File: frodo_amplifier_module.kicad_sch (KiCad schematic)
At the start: 35 parts, among them IC1 MCP3221A5T-I_OT, IC2 INA826AID, J1 Conn_01x01_Socket, J2 Conn_01x01_Socket, J3 Conn_01x01_Socket, J4 Conn_01x01_Socket, J5 Conn_01x01_Socket, J6 Conn_01x01_Socket, J7 Conn_01x01_Socket, J8 Conn_01x01_Socket, U1 MCP602, U2 MIC5504-3.3YM5

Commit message: finished the scematics
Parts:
- removed C9: 0u1, Capacitor_SMD:C_0402_1005Metric, symbol Device:C
- removed IC1: MCP3221A5T-I_OT, Package_TO_SOT_SMD:SOT-23-5, symbol MCP3221A5T-I_OT:MCP3221A5T-I_OT
- removed J1, J2, J3, J4, J5, J6, J7, J8: Conn_01x01_Socket, Connector_Wire:SolderWirePad_1x01_SMD_1x2mm, symbol Connector:Conn_01x01_Socket
- removed R2: 10k, Resistor_SMD:R_0402_1005Metric, symbol Device:R
- removed U1: MCP602, Package_SO:SOIC-8-1EP_3.9x4.9mm_P1.27mm_EP2.29x3mm, symbol Amplifier_Operational:MCP602
- added C11: 470n, Capacitor_SMD:C_0402_1005Metric, symbol Device:C
- added C12, C13: 0u1, Capacitor_SMD:C_0402_1005Metric, symbol Device:C
- added C5: 10n, Capacitor_SMD:C_0402_1005Metric, symbol Device:C
- added C6: 2n2, Capacitor_SMD:C_0402_1005Metric, symbol Device:C
- added J? (x4): JST-GH, Connector_JST:JST_GH_BM04B-GHS-TBT_1x04-1MP_P1.25mm_Vertical, symbol Connector_Generic_MountingPin:Conn_01x04_MountingPin
- added JP2, JP3: SolderJumper_3_Open, Jumper:SolderJumper-3_P1.3mm_Open_RoundedPad1.0x1.5mm, symbol Jumper:SolderJumper_3_Open
- added R4: 10k, Resistor_SMD:R_0402_1005Metric_Pad0.72x0.64mm_HandSolder, symbol Device:R
- added U1: ADC101C021CIMM, Package_SO:SSOP-8_2.95x2.8mm_P0.65mm, symbol Analog_ADC:ADC101C021CIMM
- added U2: MCP6001-OT, Package_TO_SOT_SMD:SOT-23-5, symbol Amplifier_Operational:MCP6001-OT
- added U4: REF3033, Package_TO_SOT_SMD:SOT-23, symbol Reference_Voltage:REF3033
- C1: footprint Capacitor_SMD:C_0603_1608Metric -> Capacitor_SMD:C_0402_1005Metric
- C3: value 10u -> 4u7; footprint Capacitor_SMD:C_0603_1608Metric -> Capacitor_SMD:C_0402_1005Metric
- FB1, FB2: footprint Inductor_SMD:L_0603_1608Metric -> Inductor_SMD:L_0402_1005Metric
- IC1: renamed from IC2; footprint Package_SO:SOIC-8_3.9x4.9mm_P1.27mm -> Package_SON:WSON-8-1EP_3x3mm_P0.5mm_EP1.2x2mm
- JP1: footprint Jumper:SolderJumper-3_P1.3mm_Open_RoundedPad1.0x1.5mm_NumberLabels -> Jumper:SolderJumper-3_P1.3mm_Open_RoundedPad1.0x1.5mm
- R1: footprint Resistor_SMD:R_0402_1005Metric_Pad0.72x0.64mm_HandSolder -> Resistor_SMD:R_0402_1005Metric
- R3: value 10k -> 5k; footprint Resistor_SMD:R_0402_1005Metric -> Resistor_SMD:R_0402_1005Metric_Pad0.72x0.64mm_HandSolder
- RG1: footprint Resistor_SMD:R_0603_1608Metric_Pad0.98x0.95mm_HandSolder -> Resistor_SMD:R_0603_1608Metric
- renumbered C8 to C10, C10 to C14, C11 to C15, C12 to C16, C5 to C7, C6 to C8, C7 to C9, JP2 to JP4, R4 to R2, U2 to U3
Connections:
- net +IN: now also J?.3 (Pin_3)
- net -IN: now also J?.2 (Pin_2)
- net 3V3: now also C8.1, J?.4 (Pin_4), JP2.3 (B), JP3.3 (B); no longer C3.1, C4.1, JP1.3 (B), R3.1, R5.2
- net 5V: now also C11.1, C12.1, C5.1, J?.4 (Pin_4), U4.1 (IN); no longer JP1.2 (C)
- net GND: now also C11.2, C12.2, C13.2, C5.2, C6.2, J?.1 (Pin_1), J?.1 (Pin_1), J?.2 (Pin_2), JP2.1 (A), JP3.1 (A), R4.1, U1.7 (GND), U2.2 (V-), U4.3 (GND)
- net SCL: now also J?.3 (Pin_3), J?.3 (Pin_3), U1.8 (SDA); no longer R3.2
- net SDA: now also J?.2 (Pin_2), J?.2 (Pin_2), U1.1 (SCL)
- net sig: now also JP1.3 (B)
- net sig2: now reaches JP1.1 (A)
- net sig2: now also R3.1, R4.2; no longer C8.1
- net at FB2.1: now also J?.1 (Pin_1), J?.1 (Pin_1)
- net at R5.1, R6.2: now also U2.3 (+)
- net at JP4.3 (B): now also U2.1, U2.4 (-)
- net at FB1.1: now also J?.4 (Pin_4), J?.4 (Pin_4)
- new net: JP2.2 (C), U1.3 (ADR0)
- new net: JP1.2 (C), U1.4 (VIN)
- new net: JP3.2 (C), U1.6 (ADR1)
- new net: C6.1, J?.3 (Pin_3), R3.2
- new net 3V3Ref: C13.1, C3.1, C4.1, R5.2, U1.5 (VA), U2.5 (V+), U4.2 (OUT)
- no-connect marks 0 -> 1
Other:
- note added: "pullup resistors, typically: - 10 kΩ for 100 kHz - 2 kΩ for 400 kHz SCL clock speeds -> already on io board (4.7k) -> so not neccesarry"
- note added: "to next amp board"
- note added: "to sensor (3.3V)"
- note added: "to sensor 5V"
- note removed: "possibility to supply 5V (may be neccesarry for some sensors)"
- note removed: "pullup resistors, typically: - 10 kΩ for 100 kHz - 2 kΩ for 400 kHz SCL clock speeds"
- note removed: "to sensor"
- moved on the sheet: C1, C10, C14, C15, C16, C2, C3, C4, C7, C8, C9, FB1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

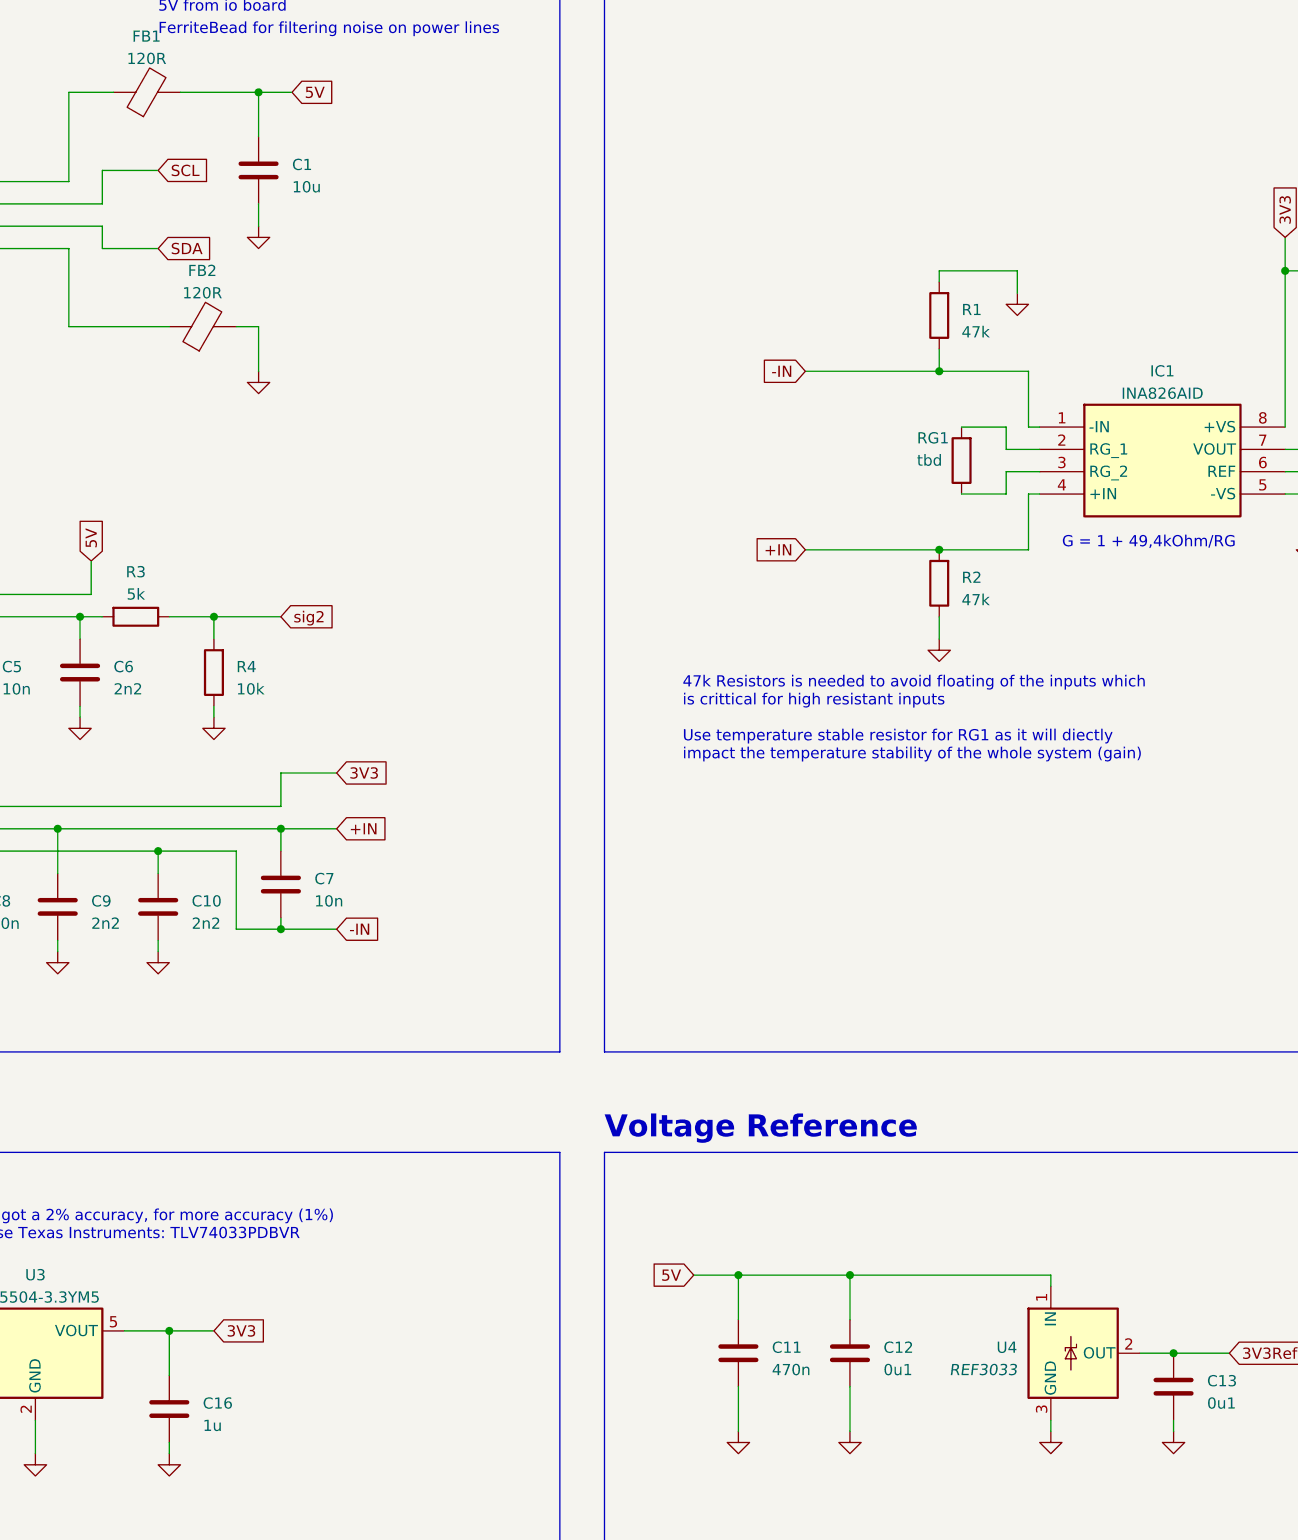
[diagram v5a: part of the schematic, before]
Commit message: started the pcb layout for the amp module
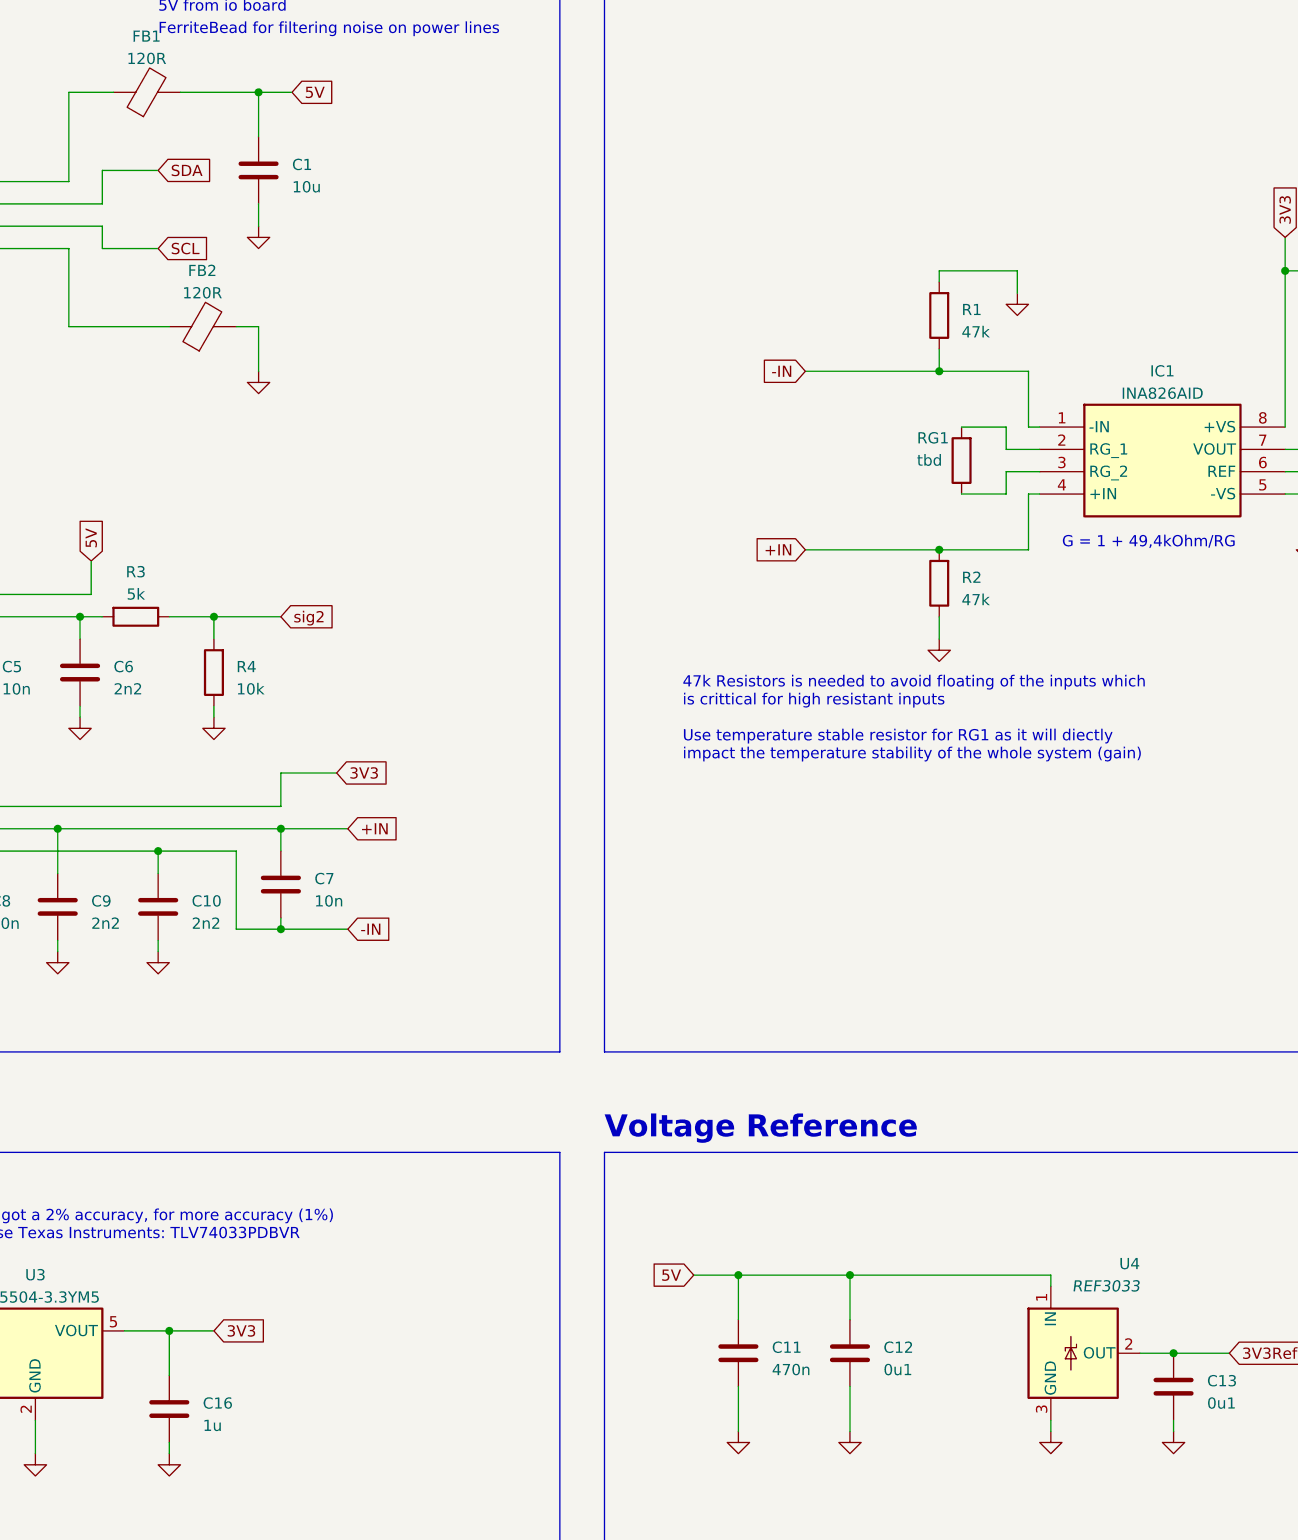
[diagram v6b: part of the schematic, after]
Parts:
- J? (x4): footprint Connector_JST:JST_GH_BM04B-GHS-TBT_1x04-1MP_P1.25mm_Vertical -> Connector_JST:JST_GH_SM04B-GHS-TB_1x04-1MP_P1.25mm_Horizontal
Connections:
- net SCL: now also J?.2 (Pin_2), J?.2 (Pin_2); no longer J?.3 (Pin_3), J?.3 (Pin_3)
- net SDA: now also J?.3 (Pin_3), J?.3 (Pin_3); no longer J?.2 (Pin_2), J?.2 (Pin_2)
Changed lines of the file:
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@@
     (stroke (width 0) (type default))
   )
-  (wire (pts (xy 100.33 138.43) (xy 106.68 138.43))
+  (wire (pts (xy 100.33 138.43) (xy 107.95 138.43))
     (stroke (width 0) (type default))
   )
@@
     (stroke (width 0) (type default))
   )
-  (wire (pts (xy 100.33 127) (xy 106.68 127))
+  (wire (pts (xy 100.33 127) (xy 107.95 127))
     (stroke (width 0) (type default))
   )
@@
     )
   )
-  (global_label "SCL" (shape input) (at 86.36 52.07 0) (fields_autoplaced)
-    (effects (font (size 1.27 1.27)) (justify left))
-    (property "Intersheetrefs" "${INTERSHEET_REFS}" (at 92.7734 52.07 0)
-      (effects (font (size 1.27 1.27)) (justify left) hide)
-    )
-  )
   (global_label "SCL" (shape input) (at 336.55 87.63 0) (fields_autoplaced)
     (effects (font (size 1.27 1.27)) (justify left))
@@
     )
   )
-  (global_label "-IN" (shape input) (at 106.68 138.43 0) (fields_autoplaced)
-    (effects (font (size 1.27 1.27)) (justify left))
-    (property "Intersheetrefs" "${INTERSHEET_REFS}" (at 113.0935 138.43 0)
-      (effects (font (size 1.27 1.27)) (justify left) hide)
-    )
-  )
   (global_label "sig2" (shape input) (at 257.81 87.63 180) (fields_autoplaced)
     (effects (font (size 1.27 1.27)) (justify right))
@@
     )
   )
+  (global_label "-IN" (shape input) (at 107.95 138.43 0) (fields_autoplaced)
+    (effects (font (size 1.27 1.27)) (justify left))
+    (property "Intersheetrefs" "${INTERSHEET_REFS}" (at 114.3635 138.43 0)
+      (effects (font (size 1.27 1.27)) (justify left) hide)
+    )
+  )
   (global_label "ref" (shape input) (at 227.33 87.63 0) (fields_autoplaced)
     (effects (font (size 1.27 1.27)) (justify left))
@@
     )
   )
+  (global_label "SCL" (shape input) (at 86.36 60.96 0) (fields_autoplaced)
+    (effects (font (size 1.27 1.27)) (justify left))
+    (property "Intersheetrefs" "${INTERSHEET_REFS}" (at 92.7734 60.96 0)
+      (effects (font (size 1.27 1.27)) (justify left) hide)
+    )
+  )
+  (global_label "SDA" (shape input) (at 86.36 52.07 0) (fields_autoplaced)
+    (effects (font (size 1.27 1.27)) (justify left))
+    (property "Intersheetrefs" "${INTERSHEET_REFS}" (at 92.8339 52.07 0)
+      (effects (font (size 1.27 1.27)) (justify left) hide)
+    )
+  )
   (global_label "SDA" (shape input) (at 336.55 82.55 0) (fields_autoplaced)
     (effects (font (size 1.27 1.27)) (justify left))
@@
     )
   )
-  (global_label "SDA" (shape input) (at 86.36 60.96 0) (fields_autoplaced)
-    (effects (font (size 1.27 1.27)) (justify left))
-    (property "Intersheetrefs" "${INTERSHEET_REFS}" (at 92.8339 60.96 0)
-      (effects (font (size 1.27 1.27)) (justify left) hide)
-    )
-  )
   (global_label "sig2" (shape input) (at 100.33 102.87 0) (fields_autoplaced)
     (effects (font (size 1.27 1.27)) (justify left))
@@
     )
   )
-  (global_label "+IN" (shape input) (at 106.68 127 0) (fields_autoplaced)
-    (effects (font (size 1.27 1.27)) (justify left))
-    (property "Intersheetrefs" "${INTERSHEET_REFS}" (at 113.0935 127 0)
-      (effects (font (size 1.27 1.27)) (justify left) hide)
-    )
-  )
   (global_label "ref" (shape input) (at 269.24 196.85 0) (fields_autoplaced)
     (effects (font (size 1.27 1.27)) (justify left))
@@
     )
   )
+  (global_label "+IN" (shape input) (at 107.95 127 0) (fields_autoplaced)
+    (effects (font (size 1.27 1.27)) (justify left))
+    (property "Intersheetrefs" "${INTERSHEET_REFS}" (at 114.3635 127 0)
+      (effects (font (size 1.27 1.27)) (justify left) hide)
+    )
+  )
   (symbol (lib_id "Reference_Voltage:REF3033") (at 190.5 186.69 0) (unit 1)
-    (in_bom yes) (on_board yes) (dnp no) (fields_autoplaced)
-    (property "Reference" "U4" (at 184.15 186.055 0)
+    (in_bom yes) (on_board yes) (dnp no)
+    (property "Reference" "U4" (at 198.12 176.53 0)
       (effects (font (size 1.27 1.27)) (justify right))
     )
-    (property "Value" "REF3033" (at 184.15 188.595 0)
+    (property "Value" "REF3033" (at 198.12 179.07 0)
       (effects (font (size 1.27 1.27) italic) (justify right))
     )
@@
       (effects (font (size 1.27 1.27)) (justify left))
     )
-    (property "Footprint" "Connector_JST:JST_GH_BM04B-GHS-TBT_1x04-1MP_P1.25mm_Vertical" (at 43.18 129.54 0)
+    (property "Footprint" "Connector_JST:JST_GH_SM04B-GHS-TB_1x04-1MP_P1.25mm_Horizontal" (at 43.18 129.54 0)
       (effects (font (size 1.27 1.27)) hide)
     )
@@
       (effects (font (size 1.27 1.27)) (justify left))
     )
-    (property "Footprint" "Connector_JST:JST_GH_BM04B-GHS-TBT_1x04-1MP_P1.25mm_Vertical" (at 45.72 58.42 0)
+    (property "Footprint" "Connector_JST:JST_GH_SM04B-GHS-TB_1x04-1MP_P1.25mm_Horizontal" (at 45.72 58.42 0)
       (effects (font (size 1.27 1.27)) hide)
     )
@@
       (effects (font (size 1.27 1.27)) (justify left))
     )
-    (property "Footprint" "Connector_JST:JST_GH_BM04B-GHS-TBT_1x04-1MP_P1.25mm_Vertical" (at 43.18 105.41 0)
+    (property "Footprint" "Connector_JST:JST_GH_SM04B-GHS-TB_1x04-1MP_P1.25mm_Horizontal" (at 43.18 105.41 0)
       (effects (font (size 1.27 1.27)) hide)
     )
@@
       (effects (font (size 1.27 1.27)) (justify left))
     )
-    (property "Footprint" "Connector_JST:JST_GH_BM04B-GHS-TBT_1x04-1MP_P1.25mm_Vertical" (at 45.72 76.2 0)
-      (effects (font (size 1.27 1.27)) hide)
-    )
+    (property "Footprint" "Connector_JST:JST_GH_SM04B-GHS-TB_1x04-1MP_P1.25mm_Horizontal" (at 45.72 76.2 0)
+      (effects (font (size 1.27 1.27)) hide)
+    )
